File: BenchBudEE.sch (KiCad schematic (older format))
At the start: 0 parts

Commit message: 3.8 Understanding The LED Driver Module
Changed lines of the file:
@@
 LIBS:BenchBudEE
 LIBS:BenchBudEE-cache
-EELAYER 24 0
+EELAYER 27 0
 EELAYER END
 $Descr A4 11693 8268
@@
 Sheet 1 9
 Title ""
-Date "7 feb 2014"
+Date "8 feb 2014"
 Rev ""
 Comp ""
@@
 F0 "LED_Driver" 50
 F1 "LED_Driver.sch" 50
-F2 "En" I L 7550 2800 60
-F3 "FREQ" I L 7550 3000 60
 F4 "String+" I R 9400 2800 60
 F5 "String-" O R 9400 3000 60
+F6 "LED_EN_PWM" I L 7550 2800 60
 $EndSheet
 $Sheet

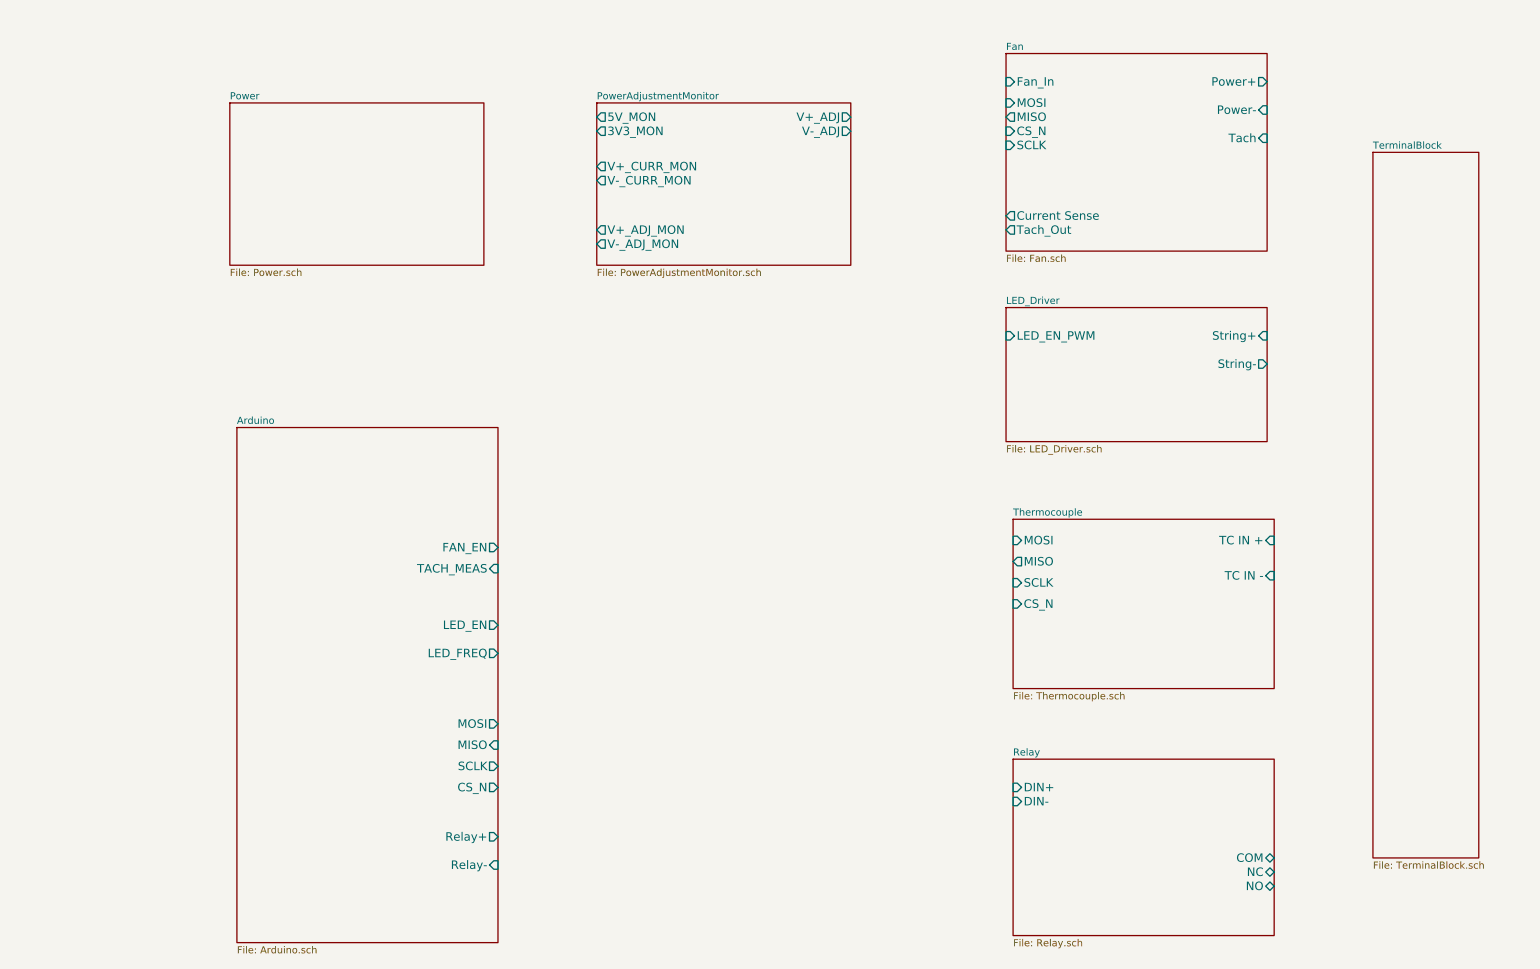
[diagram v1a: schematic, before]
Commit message: 3.9 Understanding The Arduino Module Added content to Arduino and block (header) modules
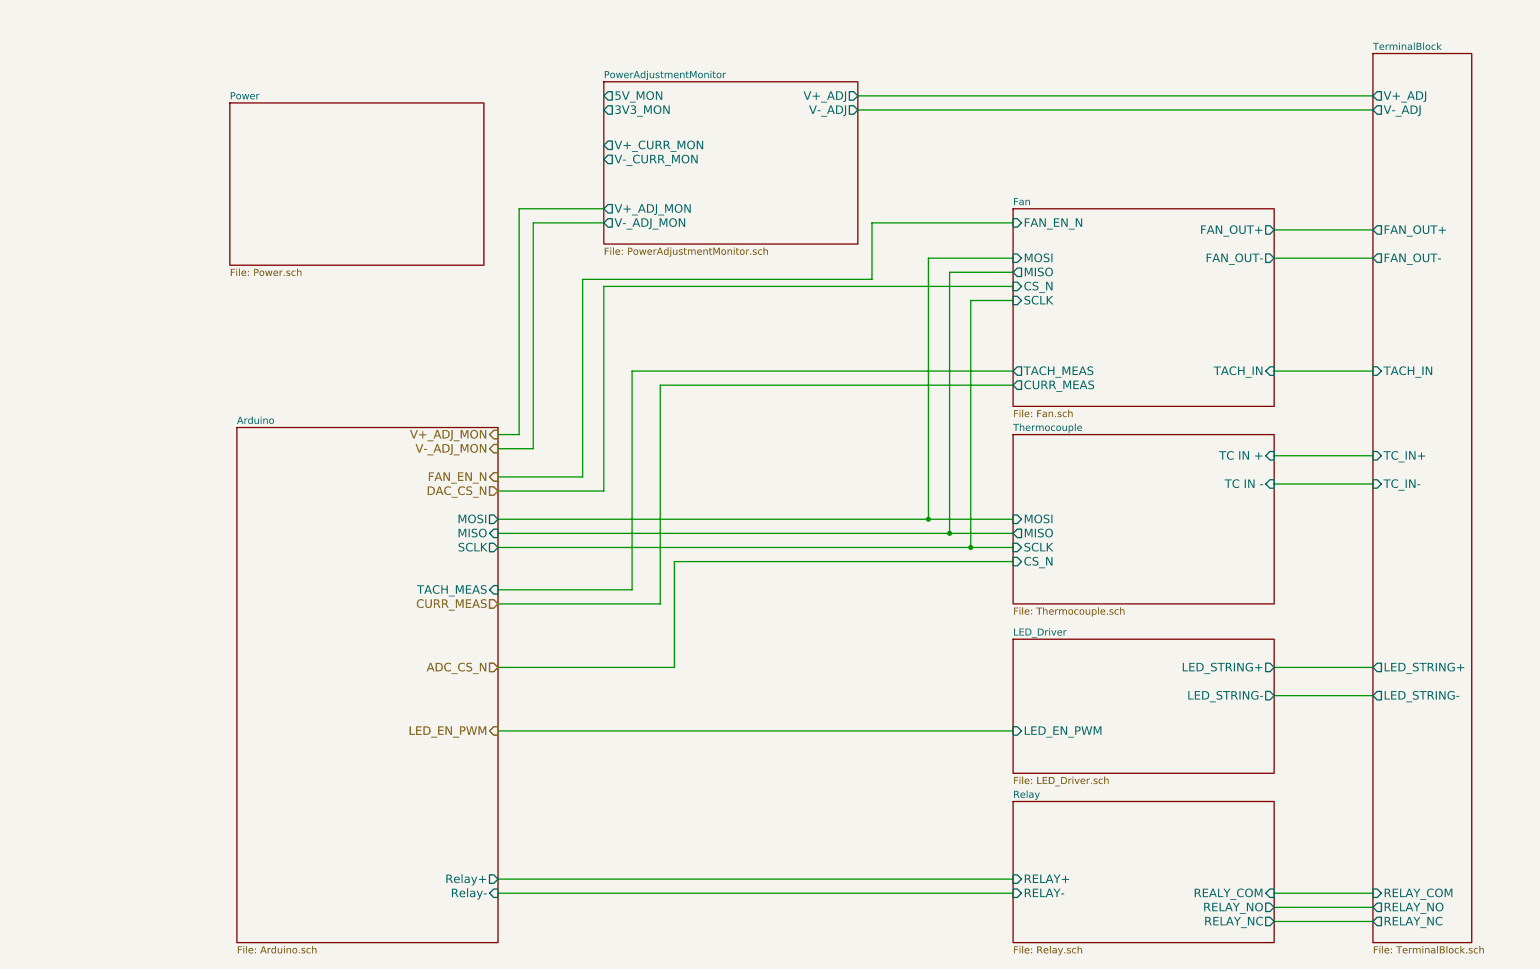
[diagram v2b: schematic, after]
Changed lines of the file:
@@
 Sheet 1 9
 Title ""
-Date "8 feb 2014"
+Date "10 feb 2014"
 Rev ""
 Comp ""
@@
 $EndDescr
 $Sheet
+S 7600 6100 1850 1000
+U 52EBE7E0
+F0 "Relay" 50
+F1 "Relay.sch" 50
+F2 "RELAY_NC" O R 9450 6950 60
+F3 "RELAY_NO" O R 9450 6850 60
+F4 "REALY_COM" I R 9450 6750 60
+F5 "RELAY+" I L 7600 6650 60
+F6 "RELAY-" I L 7600 6750 60
+$EndSheet
+$Sheet
+S 2050 1150 1800 1150
+U 52EBE800
+F0 "Power" 50
+F1 "Power.sch" 50
+$EndSheet
+$Sheet
+S 7600 4950 1850 950
+U 52EBE838
+F0 "LED_Driver" 50
+F1 "LED_Driver.sch" 50
+F2 "LED_EN_PWM" I L 7600 5600 60
+F3 "LED_STRING+" O R 9450 5150 60
+F4 "LED_STRING-" O R 9450 5350 60
+$EndSheet
+$Sheet
+S 10150 800  700  6300
+U 52EBE87D
+F0 "TerminalBlock" 50
+F1 "TerminalBlock.sch" 50
+F2 "V+_ADJ" O L 10150 1100 60
+F3 "V-_ADJ" O L 10150 1200 60
+F4 "FAN_OUT+" O L 10150 2050 60
+F5 "FAN_OUT-" O L 10150 2250 60
+F6 "TACH_IN" I L 10150 3050 60
+F7 "TC_IN+" I L 10150 3650 60
+F8 "TC_IN-" I L 10150 3850 60
+F9 "LED_STRING+" O L 10150 5150 60
+F10 "LED_STRING-" O L 10150 5350 60
+F11 "RELAY_COM" I L 10150 6750 60
+F12 "RELAY_NO" O L 10150 6850 60
+F13 "RELAY_NC" O L 10150 6950 60
+$EndSheet
+$Sheet
+S 4700 1000 1800 1150
+U 52F44BE7
+F0 "PowerAdjustmentMonitor" 50
+F1 "PowerAdjustmentMonitor.sch" 50
+F2 "V-_ADJ" O R 6500 1200 60
+F3 "3V3_MON" O L 4700 1200 60
+F4 "V+_ADJ_MON" O L 4700 1900 60
+F5 "V-_ADJ_MON" O L 4700 2000 60
+F6 "V+_CURR_MON" O L 4700 1450 60
+F7 "V-_CURR_MON" O L 4700 1550 60
+F8 "V+_ADJ" O R 6500 1100 60
+F9 "5V_MON" O L 4700 1100 60
+$EndSheet
+$Sheet
+S 7600 1900 1850 1400
+U 52EBE84E
+F0 "Fan" 50
+F1 "Fan.sch" 50
+F2 "FAN_OUT+" O R 9450 2050 60
+F3 "FAN_OUT-" O R 9450 2250 60
+F4 "MOSI" I L 7600 2250 60
+F5 "MISO" O L 7600 2350 60
+F6 "CS_N" I L 7600 2450 60
+F7 "SCLK" I L 7600 2550 60
+F8 "TACH_MEAS" O L 7600 3050 60
+F9 "FAN_EN_N" I L 7600 2000 60
+F10 "CURR_MEAS" O L 7600 3150 60
+F11 "TACH_IN" I R 9450 3050 60
+$EndSheet
+Wire Wire Line
+	10150 1100 6500 1100
+Wire Wire Line
+	6500 1200 10150 1200
+Wire Wire Line
+	9450 2050 10150 2050
+Wire Wire Line
+	10150 2250 9450 2250
+Wire Wire Line
+	10150 3050 9450 3050
+Wire Wire Line
+	9450 3650 10150 3650
+Wire Wire Line
+	10150 3850 9450 3850
+Wire Wire Line
+	9450 5150 10150 5150
+Wire Wire Line
+	10150 5350 9450 5350
+Wire Wire Line
+	9450 6750 10150 6750
+Wire Wire Line
+	9450 6850 10150 6850
+Wire Wire Line
+	9450 6950 10150 6950
+Text HLabel 3950 3500 0    60   Output ~ 0
+V+_ADJ_MON
+Text HLabel 3950 3600 0    60   Output ~ 0
+V-_ADJ_MON
+Text HLabel 3950 3800 0    60   Output ~ 0
+FAN_EN_N
+Text HLabel 3950 3900 0    60   Input ~ 0
+DAC_CS_N
+Text HLabel 3950 4700 0    60   Input ~ 0
+CURR_MEAS
+Text HLabel 3950 5150 0    60   Input ~ 0
+ADC_CS_N
+Text HLabel 3950 5600 0    60   Output ~ 0
+LED_EN_PWM
+Wire Wire Line
+	3950 6650 7600 6650
+Wire Wire Line
+	3950 6750 7600 6750
+$Sheet
+S 7600 3500 1850 1200
+U 52EBE76F
+F0 "Thermocouple" 50
+F1 "Thermocouple.sch" 50
+F2 "TC IN +" I R 9450 3650 60
+F3 "TC IN -" I R 9450 3850 60
+F4 "MOSI" I L 7600 4100 60
+F5 "MISO" O L 7600 4200 60
+F6 "SCLK" I L 7600 4300 60
+F7 "CS_N" I L 7600 4400 60
+$EndSheet
+Wire Wire Line
+	3950 3500 4100 3500
+Wire Wire Line
+	4100 3500 4100 1900
+Wire Wire Line
+	4100 1900 4700 1900
+Wire Wire Line
+	4700 2000 4200 2000
+Wire Wire Line
+	4200 2000 4200 3600
+Wire Wire Line
+	4200 3600 3950 3600
+Wire Wire Line
+	6600 2000 7600 2000
+Wire Wire Line
+	3950 3800 4550 3800
+Wire Wire Line
+	4550 3800 4550 2400
+Wire Wire Line
+	4550 2400 6600 2400
+Wire Wire Line
+	6600 2400 6600 2000
+Wire Wire Line
+	3950 3900 4700 3900
+Wire Wire Line
+	4700 3900 4700 2450
+Wire Wire Line
+	4700 2450 7600 2450
+$Sheet
 S 2100 3450 1850 3650
 U 52EBE680
 F0 "Arduino" 50
 F1 "Arduino.sch" 50
-F2 "Relay+" O R 3950 6350 60
-F3 "Relay-" I R 3950 6550 60
-F4 "MOSI" O R 3950 5550 60
-F5 "MISO" I R 3950 5700 60
-F6 "SCLK" O R 3950 5850 60
-F7 "CS_N" O R 3950 6000 60
-F8 "LED_EN" O R 3950 4850 60
-F9 "LED_FREQ" O R 3950 5050 60
-F10 "FAN_EN" O R 3950 4300 60
-F11 "TACH_MEAS" I R 3950 4450 60
-$EndSheet
-$Sheet
-S 7600 5800 1850 1250
-U 52EBE7E0
-F0 "Relay" 50
-F1 "Relay.sch" 50
-F2 "NC" B R 9450 6600 60
-F3 "NO" B R 9450 6700 60
-F4 "COM" B R 9450 6500 60
-F5 "DIN+" I L 7600 6000 60
-F6 "DIN-" I L 7600 6100 60
-$EndSheet
-$Sheet
-S 2050 1150 1800 1150
-U 52EBE800
-F0 "Power" 50
-F1 "Power.sch" 50
-$EndSheet
-$Sheet
-S 7550 2600 1850 950
-U 52EBE838
-F0 "LED_Driver" 50
-F1 "LED_Driver.sch" 50
-F4 "String+" I R 9400 2800 60
-F5 "String-" O R 9400 3000 60
-F6 "LED_EN_PWM" I L 7550 2800 60
-$EndSheet
-$Sheet
-S 10150 1500 750  5000
-U 52EBE87D
-F0 "TerminalBlock" 50
-F1 "TerminalBlock.sch" 50
-$EndSheet
-$Sheet
-S 7600 4100 1850 1200
-U 52EBE76F
-F0 "Thermocouple" 50
-F1 "Thermocouple.sch" 50
-F2 "TC IN +" I R 9450 4250 60
-F3 "TC IN -" I R 9450 4500 60
-F4 "MOSI" I L 7600 4250 60
-F5 "MISO" O L 7600 4400 60
-F6 "SCLK" I L 7600 4550 60
-F7 "CS_N" I L 7600 4700 60
-$EndSheet
-$Sheet
-S 7550 800  1850 1400
-U 52EBE84E
-F0 "Fan" 50
-F1 "Fan.sch" 50
-F2 "Power+" O R 9400 1000 60
-F3 "Power-" I R 9400 1200 60
-F4 "Tach" I R 9400 1400 60
-F5 "Tach_Out" O L 7550 2050 60
-F6 "Fan_In" I L 7550 1000 60
-F7 "Current Sense" O L 7550 1950 60
-F8 "MOSI" I L 7550 1150 60
-F9 "MISO" O L 7550 1250 60
-F10 "CS_N" I L 7550 1350 60
-F11 "SCLK" I L 7550 1450 60
-$EndSheet
-$Sheet
-S 4650 1150 1800 1150
-U 52F44BE7
-F0 "PowerAdjustmentMonitor" 50
-F1 "PowerAdjustmentMonitor.sch" 50
-F2 "V-_ADJ" O R 6450 1350 60
-F3 "3V3_MON" O L 4650 1350 60
-F4 "V+_ADJ_MON" O L 4650 2050 60
-F5 "V-_ADJ_MON" O L 4650 2150 60
-F6 "V+_CURR_MON" O L 4650 1600 60
-F7 "V-_CURR_MON" O L 4650 1700 60
-F8 "V+_ADJ" O R 6450 1250 60
-F9 "5V_MON" O L 4650 1250 60
-$EndSheet
+F2 "Relay+" O R 3950 6650 60
+F3 "Relay-" I R 3950 6750 60
+F4 "MOSI" O R 3950 4100 60
+F5 "MISO" I R 3950 4200 60
+F6 "SCLK" O R 3950 4300 60
+F7 "TACH_MEAS" I R 3950 4600 60
+$EndSheet
+Wire Wire Line
+	3950 4600 4900 4600
+Wire Wire Line
+	4900 4600 4900 3050
+Wire Wire Line
+	4900 3050 7600 3050
+Wire Wire Line
+	3950 4700 5100 4700
+Wire Wire Line
+	5100 4700 5100 3150
+Wire Wire Line
+	5100 3150 7600 3150
+Wire Wire Line
+	5200 5150 3950 5150
+Wire Wire Line
+	3950 5600 7600 5600
+Wire Wire Line
+	3950 4100 7600 4100
+Wire Wire Line
+	3950 4200 7600 4200
+Wire Wire Line
+	7600 4300 3950 4300
+Wire Wire Line
+	5200 5150 5200 4400
+Wire Wire Line
+	5200 4400 7600 4400
+Wire Wire Line
+	7600 2250 7000 2250
+Wire Wire Line
+	7000 2250 7000 4100
+Connection ~ 7000 4100
+Wire Wire Line
+	7600 2350 7150 2350
+Wire Wire Line
+	7150 2350 7150 4200
+Connection ~ 7150 4200
+Wire Wire Line
+	7600 2550 7300 2550
+Wire Wire Line
+	7300 2550 7300 4300
+Connection ~ 7300 4300
 $EndSCHEMATC

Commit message: 3.10   Revisiting The Current/Fan Module End of Module 3, lots of cleanup/changes all over the place.
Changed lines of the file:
@@
 F7 "SCLK" I L 7600 2550 60
 F8 "TACH_MEAS" O L 7600 3050 60
-F9 "FAN_EN_N" I L 7600 2000 60
-F10 "CURR_MEAS" O L 7600 3150 60
-F11 "TACH_IN" I R 9450 3050 60
+F9 "CURR_MEAS" O L 7600 3150 60
+F10 "TACH_IN" I R 9450 3050 60
+F11 "FAN_PWN" I L 7600 2000 60
+F12 "FAN_MODE" O L 7600 2950 60
 $EndSheet
 Wire Wire Line
@@
 	4100 1900 4700 1900
 Wire Wire Line
-	4700 2000 4200 2000
+	4700 2000 4150 2000
 Wire Wire Line
-	4200 2000 4200 3600
+	4150 2000 4150 3600
 Wire Wire Line
-	4200 3600 3950 3600
+	4150 3600 3950 3600
 Wire Wire Line
 	6600 2000 7600 2000
@@
 	3950 3800 4550 3800
 Wire Wire Line
-	4550 3800 4550 2400
+	4550 3800 4550 2300
 Wire Wire Line
-	4550 2400 6600 2400
+	4550 2300 6600 2300
 Wire Wire Line
-	6600 2400 6600 2000
+	6600 2300 6600 2000
 Wire Wire Line
-	3950 3900 4700 3900
+	3950 3900 4600 3900
 Wire Wire Line
-	4700 3900 4700 2450
+	4600 3900 4600 2450
 Wire Wire Line
-	4700 2450 7600 2450
+	4600 2450 7600 2450
 $Sheet
 S 2100 3450 1850 3650
@@
 $EndSheet
 Wire Wire Line
-	3950 4600 4900 4600
+	3950 4600 4950 4600
 Wire Wire Line
-	4900 4600 4900 3050
+	4950 4600 4950 3050
 Wire Wire Line
-	4900 3050 7600 3050
+	4950 3050 7600 3050
 Wire Wire Line
-	3950 4700 5100 4700
+	3950 4700 5000 4700
 Wire Wire Line
-	5100 4700 5100 3150
+	5000 4700 5000 3150
 Wire Wire Line
-	5100 3150 7600 3150
+	5000 3150 7600 3150
 Wire Wire Line
-	5200 5150 3950 5150
+	5550 5150 3950 5150
 Wire Wire Line
 	3950 5600 7600 5600
 Wire Wire Line
-	3950 4100 7600 4100
+	3950 4100 7000 4100
 Wire Wire Line
-	3950 4200 7600 4200
+	7000 4100 7600 4100
 Wire Wire Line
-	7600 4300 3950 4300
+	3950 4200 7150 4200
 Wire Wire Line
-	5200 5150 5200 4400
+	7150 4200 7600 4200
 Wire Wire Line
-	5200 4400 7600 4400
+	7600 4300 7300 4300
+Wire Wire Line
+	7300 4300 3950 4300
+Wire Wire Line
+	5550 5150 5550 4400
+Wire Wire Line
+	5550 4400 7600 4400
 Wire Wire Line
 	7600 2250 7000 2250
@@
 	7300 2550 7300 4300
 Connection ~ 7300 4300
+Wire Wire Line
+	7600 2950 4900 2950
+Wire Wire Line
+	4900 2950 4900 4500
+Wire Wire Line
+	4900 4500 3950 4500
+Text HLabel 3950 4500 0    60   Output ~ 0
+FAN_MODE
 $EndSCHEMATC

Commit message: 5.3 Video 1/2 Associating and Placing the Relay Module
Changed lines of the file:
@@
 Sheet 1 9
 Title ""
-Date "10 feb 2014"
+Date "19 feb 2014"
 Rev ""
 Comp ""
@@
 	3950 5600 7600 5600
 Wire Wire Line
-	3950 4100 7000 4100
-Wire Wire Line
-	7000 4100 7600 4100
-Wire Wire Line
-	3950 4200 7150 4200
-Wire Wire Line
-	7150 4200 7600 4200
-Wire Wire Line
-	7600 4300 7300 4300
-Wire Wire Line
-	7300 4300 3950 4300
+	3950 4100 7600 4100
+Wire Wire Line
+	3950 4200 7600 4200
+Wire Wire Line
+	3950 4300 7600 4300
 Wire Wire Line
 	5550 5150 5550 4400
